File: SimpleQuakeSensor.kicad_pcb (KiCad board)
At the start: 2 copper layers, 39.9 x 22 mm, 37 parts, among them J1 Conn_Coaxial_Small, J2 Conn_Coaxial_Small, J3 Bat -12V GND, J4 Bat +12V, Q1 2N4401, Q2 BF245B, Q3 2N4401

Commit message: Add blocking capacitor
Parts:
- added C14: 10 uF, Capacitor_Tantalum_SMD:CP_EIA-2012-12_Kemet-R, F.Cu at (166.1, 91.7)
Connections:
- C11 pad 1: Net-(J2-In) -> Net-(Q3-C)
- Q3 pad 3: Net-(J2-In) -> Net-(Q3-C)
- R8 pad 1: Net-(J2-In) -> Net-(Q3-C)
- R9 pad 2: Net-(J2-In) -> Net-(Q3-C)
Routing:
- net Net-(J2-In): track 18.6 -> 3.71 mm
- net Net-(Q3-C): track 0.00 -> 14.2 mm

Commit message: Better impedance matching
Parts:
- C10: value 10 nF -> 47 nF
- C11, C7: value 1 nF -> 2.2 nF
- C3: value 1 nF -> 47 nF
- R8: value 10 M -> 2.2 M
- R9: value 100 K -> 22 K
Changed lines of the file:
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@@
 			)
 		)
-		(property "Value" "10 M"
+		(property "Value" "2.2 M"
 			(at 0 1.65 0)
 			(layer "F.Fab")
@@
 			)
 		)
-		(property "Value" "1 nF"
+		(property "Value" "2.2 nF"
 			(at 0 1.68 90)
 			(layer "F.Fab")
@@
 			)
 		)
-		(property "Value" "1 nF"
+		(property "Value" "47 nF"
 			(at 0 1.68 0)
 			(layer "F.Fab")
@@
 			)
 		)
-		(property "Value" "100 K"
+		(property "Value" "22 K"
 			(at 0 1.65 90)
 			(layer "F.Fab")
@@
 			)
 		)
-		(property "Value" "1 nF"
+		(property "Value" "2.2 nF"
 			(at 0 1.68 90)
 			(layer "F.Fab")
@@
 			)
 		)
-		(property "Value" "10 nF"
+		(property "Value" "47 nF"
 			(at 0 1.68 90)
 			(layer "F.Fab")
@@
 	)
 	(segment
-		(start 169.753212 90.621533)
-		(end 166.298467 90.621533)
+		(start 159.543212 94.751533)
+		(end 162.500712 94.751533)
 		(width 1)
 		(layer "F.Cu")
-		(net "Net-(J2-In)")
+		(net "Net-(Q3-C)")
 	)
 	(segment
-		(start 166.298467 90.621533)
-		(end 166.12 90.8)
+		(start 162.500712 94.751533)
+		(end 163.665712 93.586533)
 		(width 1)
 		(layer "F.Cu")
-		(net "Net-(J2-In)")
+		(net "Net-(Q3-C)")
+	)
+	(segment
+		(start 163.623212 95.981533)
+		(end 163.633212 95.971533)
+		(width 1)
+		(layer "F.Cu")
+		(net "Net-(Q3-C)")
+	)
+	(segment
+		(start 158.623212 92.999033)
+		(end 158.790712 92.831533)
+		(width 1)
+		(layer "F.Cu")
+		(net "Net-(Q3-C)")
+	)
+	(segment
+		(start 158.790712 93.999033)
+		(end 159.543212 94.751533)
+		(width 1)
+		(layer "F.Cu")
+		(net "Net-(Q3-C)")
+	)
+	(segment
+		(start 165.113467 93.586533)
+		(end 166.12 92.58)
+		(width 1)
+		(layer "F.Cu")
+		(net "Net-(Q3-C)")
+	)
+	(segment
+		(start 163.633212 94.059033)
+		(end 163.563212 93.989033)
+		(width 1)
+		(layer "F.Cu")
+		(net "Net-(Q3-C)")
+	)
+	(segment
+		(start 163.665712 93.586533)
+		(end 165.113467 93.586533)
+		(width 1)
+		(layer "F.Cu")
+		(net "Net-(Q3-C)")
+	)
+	(segment
+		(start 156.393212 92.999033)
+		(end 158.623212 92.999033)
+		(width 1)
+		(layer "F.Cu")
+		(net "Net-(Q3-C)")
+	)
+	(segment
+		(start 163.633212 95.971533)
+		(end 163.633212 94.059033)
+		(width 1)
+		(layer "F.Cu")
+		(net "Net-(Q3-C)")
+	)
+	(segment
+		(start 158.790712 92.831533)
+		(end 158.790712 93.999033)
+		(width 1)
+		(layer "F.Cu")
+		(net "Net-(Q3-C)")
 	)
 	(segment
@@
 	)
 	(segment
+		(start 169.753212 90.621533)
+		(end 166.298467 90.621533)
+		(width 1)
+		(layer "F.Cu")
+		(net "Net-(J2-In)")
+	)
+	(segment
+		(start 166.298467 90.621533)
+		(end 166.12 90.8)
+		(width 1)
+		(layer "F.Cu")
+		(net "Net-(J2-In)")
+	)
+	(segment
 		(start 148.618212 88.211533)
 		(end 145.493212 88.211533)
@@
 		(net "Net-(J1-Ext)")
 	)
-	(segment
-		(start 159.543212 94.751533)
-		(end 162.500712 94.751533)
-		(width 1)
-		(layer "F.Cu")
-		(net "Net-(Q3-C)")
-	)
-	(segment
-		(start 162.500712 94.751533)
-		(end 163.665712 93.586533)
-		(width 1)
-		(layer "F.Cu")
-		(net "Net-(Q3-C)")
-	)
-	(segment
-		(start 163.623212 95.981533)
-		(end 163.633212 95.971533)
-		(width 1)
-		(layer "F.Cu")
-		(net "Net-(Q3-C)")
-	)
-	(segment
-		(start 158.623212 92.999033)
-		(end 158.790712 92.831533)
-		(width 1)
-		(layer "F.Cu")
-		(net "Net-(Q3-C)")
-	)
-	(segment
-		(start 158.790712 93.999033)
-		(end 159.543212 94.751533)
-		(width 1)
-		(layer "F.Cu")
-		(net "Net-(Q3-C)")
-	)
-	(segment
-		(start 165.113467 93.586533)
-		(end 166.12 92.58)
-		(width 1)
-		(layer "F.Cu")
-		(net "Net-(Q3-C)")
-	)
-	(segment
-		(start 163.633212 94.059033)
-		(end 163.563212 93.989033)
-		(width 1)
-		(layer "F.Cu")
-		(net "Net-(Q3-C)")
-	)
-	(segment
-		(start 163.665712 93.586533)
-		(end 165.113467 93.586533)
-		(width 1)
-		(layer "F.Cu")
-		(net "Net-(Q3-C)")
-	)
-	(segment
-		(start 156.393212 92.999033)
-		(end 158.623212 92.999033)
-		(width 1)
-		(layer "F.Cu")
-		(net "Net-(Q3-C)")
-	)
-	(segment
-		(start 163.633212 95.971533)
-		(end 163.633212 94.059033)
-		(width 1)
-		(layer "F.Cu")
-		(net "Net-(Q3-C)")
-	)
-	(segment
-		(start 158.790712 92.831533)
-		(end 158.790712 93.999033)
-		(width 1)
-		(layer "F.Cu")
-		(net "Net-(Q3-C)")
-	)
 	(zone

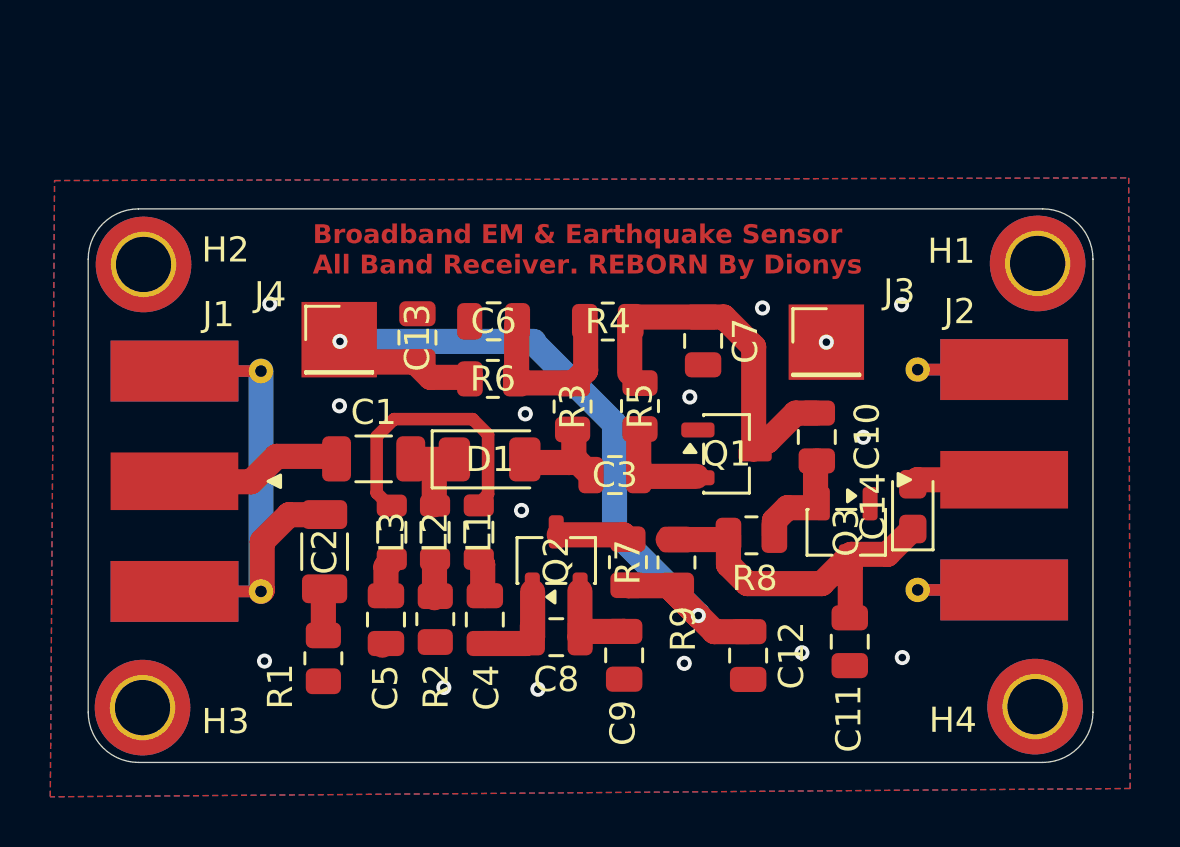
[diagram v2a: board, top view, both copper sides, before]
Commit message: Updating osc, potentiometers, models, licence logo
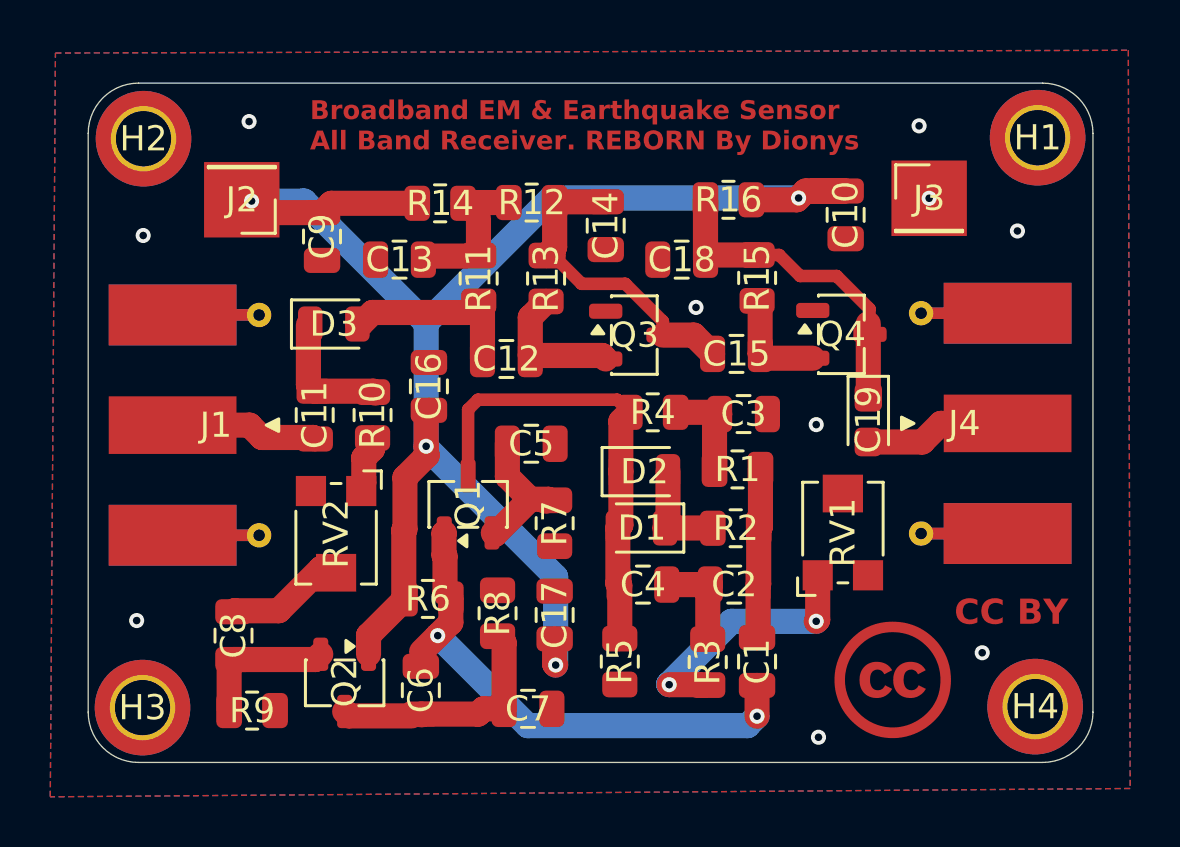
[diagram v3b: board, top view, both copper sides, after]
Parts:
- removed L1, L3: 5 mH, Inductor_SMD:L_0805_2012Metric
- removed L2: 2.2 uH, Inductor_SMD:L_0805_2012Metric
- added C15: 47 nF, Capacitor_SMD:C_0805_2012Metric, F.Cu at (159.1, 85.6)
- added C16: 100 nF, Capacitor_SMD:C_0805_2012Metric, F.Cu at (146.9, 86.9)
- added C17: 100 nF, Capacitor_SMD:C_0805_2012Metric, F.Cu at (151.9, 96.0)
- added C18: 2.2 nF, Capacitor_SMD:C_0805_2012Metric, F.Cu at (156.9, 81.9)
- added C19: 10 uF, Capacitor_Tantalum_SMD:CP_EIA-2012-15_AVX-P, F.Cu at (164.3, 88.2)
- added D2: 1N914WT, Diode_SMD:D_0805_2012Metric, F.Cu at (155.4, 90.3)
- added D3: 1N5711, Diode_SMD:D_0805_2012Metric, F.Cu at (143.1, 84.4)
- added Q4: 2N4401, Package_TO_SOT_SMD:SOT-23-3, F.Cu at (163.3, 84.8)
- added R10: 10k, Resistor_SMD:R_0805_2012Metric, F.Cu at (144.6, 88.0)
- added R11: 10 M, Resistor_SMD:R_0805_2012Metric, F.Cu at (148.9, 82.6)
- added R12: 100 K, Resistor_SMD:R_0805_2012Metric, F.Cu at (151.0, 79.6)
- added R13: 10 M, Resistor_SMD:R_0805_2012Metric, F.Cu at (151.5, 82.6)
- added R14: 10 K, Resistor_SMD:R_0805_2012Metric, F.Cu at (147.3, 79.6)
- added R15: 2.2 M, Resistor_SMD:R_0805_2012Metric, F.Cu at (159.9, 82.6)
- added R16: 22 K, Resistor_SMD:R_0805_2012Metric, F.Cu at (158.8, 79.5)
- added RV1: 1K, Potentiometer_SMD:Potentiometer_Bourns_TC33X_Vertical, F.Cu at (163.3, 92.6)
- added RV2: 1K, Potentiometer_SMD:Potentiometer_Bourns_TC33X_Vertical, F.Cu at (143.2, 92.9)
- C1: value 220 pF -> 100 nF; footprint Capacitor_SMD:C_1206_3216Metric -> Capacitor_SMD:C_0805_2012Metric
- C10, C9: value 47 nF -> 100 nF
- C11: value 2.2 nF -> 220 pF
- C12: value 100 nF -> 47 nF
- C14: value 10 uF -> 2.2 nF; footprint Capacitor_Tantalum_SMD:CP_EIA-2012-12_Kemet-R -> Capacitor_SMD:C_0805_2012Metric
- C2: value 220 pF -> 1nF; footprint Capacitor_SMD:C_1206_3216Metric -> Capacitor_SMD:C_0805_2012Metric
- C3: value 47 nF -> 2nF
- C4: value 10 nF -> 1nF
- C5: value 10 nF -> 470nF
- C6: value 100 nF -> 10nF
- C7: value 2.2 nF -> 22pF
- C8: value 47 nF -> 100nF
- D1: value 1N5711 -> 1N914WT; footprint Diode_SMD:D_1206_3216Metric -> Diode_SMD:D_0805_2012Metric
- J2: value Conn_Coaxial_Small -> Bat +12V; footprint Connector_Coaxial:SMA_Molex_73251-1153_EdgeMount_Horizontal -> fmd-laser-libs:PinHeader_1x01_P2.54mm_Vertical_2_FMD
- J4: value Bat +12V -> Conn_Coaxial_Small; footprint fmd-laser-libs:PinHeader_1x01_P2.54mm_Vertical_2_FMD -> Connector_Coaxial:SMA_Molex_73251-1153_EdgeMount_Horizontal
- Q1: value 2N4401 -> MMBFJ201
- Q2: value BF245B -> MMBFJ201
- R1: value 10k -> 6.65K
- R2: value 10k -> 470K
- R3: value 10 M -> 2.7K
- R4: value 100 K -> 6.65K
- R5: value 10 M -> 1M
- R6: value 10 K -> 10K
- R7: value 100 K -> 2.2K
- R8: value 2.2 M -> 1M
- R9: value 22 K -> 10K
- moved J2 30.7 mm to (139.4, 79.5)
- moved J4 25.1 mm to (168.2, 88.4), turned to 180 degrees
- moved C11 23.1 mm to (142.3, 88.0), turned to 90 degrees
- moved C9 20.5 mm to (142.6, 81.0)
- moved R1 18.1 mm to (159.2, 90.2), turned to 180 degrees
- moved R9 17.9 mm to (139.8, 99.8), turned to 0 degrees
- moved C1 17.2 mm to (159.9, 97.8), turned to 90 degrees
- moved C14 16.5 mm to (153.9, 80.5), turned to -90 degrees
- moved C2 16.3 mm to (159.0, 94.8), turned to 180 degrees
- moved C7 16.2 mm to (150.8, 99.7), turned to 0 degrees
- moved C12 15.2 mm to (150.0, 85.8), turned to 0 degrees
- moved C6 15.0 mm to (146.6, 99.0), turned to -90 degrees
- moved C8 12.8 mm to (139.1, 96.8), turned to 90 degrees
- moved R2 12.5 mm to (159.1, 92.5), turned to 180 degrees
- moved Q3 11.5 mm to (155.0, 84.9), turned to 0 degrees
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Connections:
- C1 pad 1: Net-(J1-In) -> Net-(Q1-D)
- C1 pad 2: Net-(D1-K) -> Net-(C1-Pad2)
- C10 pad 1: Net-(Q3-B) -> 0
- C10 pad 2: Net-(Q1-C) -> /Bat +12V
- C11 pad 1: Net-(Q3-C) -> Net-(J1-In)
- C11 pad 2: 0 -> Net-(D3-K)
- C12 pad 1: 0 -> Net-(D3-A)
- C12 pad 2: Net-(BT1-+) -> Net-(Q3-B)
- C13 pad 1: Net-(BT1-+) -> Net-(C13-Pad1)
- C14 pad 2: Net-(J2-In) -> 0
- C2 pad 1: Net-(J1-Ext) -> Net-(C1-Pad2)
- C3 pad 1: Net-(D1-A) -> 0
- C3 pad 2: Net-(Q1-B) -> Net-(C3-Pad2)
- C4 pad 1: Net-(C4-Pad1) -> Net-(C2-Pad2)
- C4 pad 2: Net-(Q2-G) -> Net-(D1-A)
- C5 pad 1: Net-(C5-Pad1) -> 0
- C5 pad 2: 0 -> Net-(Q1-S)
- C6 pad 1: Net-(C6-Pad1) -> Net-(Q1-D)
- C6 pad 2: 0 -> Net-(Q2-G)
- C7 pad 1: Net-(Q1-C) -> Net-(Q2-G)
- C8 pad 2: Net-(Q2-G) -> Net-(C8-Pad2)
- C9 pad 1: Net-(Q2-S) -> /Bat +12V
- J1 pad 2: Net-(J1-Ext) -> 0
- J2 pad 1: Net-(J2-In) -> /Bat +12V
- J4 pad 1: Net-(BT1-+) -> Net-(J4-In)
- Q1 pad 1: 0 -> Net-(Q1-D)
- Q1 pad 2: Net-(Q1-B) -> Net-(Q1-S)
- Q1 pad 3: Net-(Q1-C) -> Net-(D1-A)
- Q2 pad 1: Net-(Q2-G) -> /Bat +12V
- Q2 pad 3: Net-(Q2-D) -> Net-(Q2-G)
- R1 pad 1: Net-(C2-Pad2) -> Net-(C1-Pad2)
- R1 pad 2: 0 -> Net-(C3-Pad2)
- R2 pad 1: 0 -> Net-(C1-Pad2)
- R2 pad 2: Net-(L2-Pad1) -> Net-(D1-K)
- R3 pad 1: Net-(C6-Pad1) -> Net-(C2-Pad2)
- R3 pad 2: Net-(D1-A) -> Net-(R3-Pad2)
- R4 pad 1: Net-(C6-Pad1) -> Net-(C3-Pad2)
- R4 pad 2: Net-(Q1-C) -> Net-(D1-A)
- R5 pad 1: Net-(Q1-C) -> Net-(D1-A)
- R5 pad 2: Net-(Q1-B) -> 0
- R6 pad 1: Net-(C6-Pad1) -> /Bat +12V
- R6 pad 2: Net-(BT1-+) -> Net-(Q1-D)
- R7 pad 1: Net-(Q2-D) -> Net-(Q1-S)
- R7 pad 2: Net-(BT1-+) -> 0
- R8 pad 1: Net-(Q3-C) -> Net-(Q2-G)
- R8 pad 2: Net-(Q3-B) -> 0
- R9 pad 1: Net-(BT1-+) -> Net-(Q2-S)
- R9 pad 2: Net-(Q3-C) -> 0
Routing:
- net /Bat +12V: track 0.00 -> 65.9 mm, vias 0 -> 4
- net Net-(BT1-+): track 34.5 -> 0.00 mm, vias 2 -> 0
- net Net-(Q1-D): track 0.00 -> 20.9 mm, vias 0 -> 2
- net Net-(Q1-C): track 14.7 -> 0.00 mm
- net Net-(D1-A): track 4.30 -> 18.7 mm
- net Net-(J1-Ext): track 13.8 -> 0.00 mm
- net Net-(Q4-C): track 0.00 -> 13.3 mm
- net Net-(L1-Pad2): track 11.1 -> 0.00 mm
- net Net-(R3-Pad2): track 0.00 -> 10.3 mm, vias 0 -> 2
- net Net-(D3-A): track 0.00 -> 7.54 mm
- net Net-(C6-Pad1): track 7.18 -> 0.00 mm
- net Net-(C1-Pad2): track 0.00 -> 6.75 mm
- net Net-(J4-In): track 0.00 -> 5.85 mm
- net Net-(Q1-S): track 0.00 -> 5.57 mm
- net Net-(Q2-G): track 3.81 -> 9.18 mm
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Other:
- board size 39.9 x 22 mm -> 39.9 x 27 mm
- board text added: "CC BY"

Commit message: PCB update
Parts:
- R14: value 10 K -> 1 K
- moved J2 0.39 mm to (139.7, 79.2)
- moved Q1 0.20 mm to (148.4, 91.8)
- moved J3 0.17 mm to (166.9, 79.3)
- moved C9 0.16 mm to (142.8, 81.0)
- moved R3 0.14 mm to (157.8, 97.8)
- moved R13 0.09 mm to (151.4, 82.6)
- moved RV2 0.08 mm to (143.1, 92.9)
- moved C7 0.08 mm to (150.8, 99.8)
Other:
- board text added: "+12v"
- board text added: "GND"
- board text added: "Input (probes)"
- board text added: "Output"

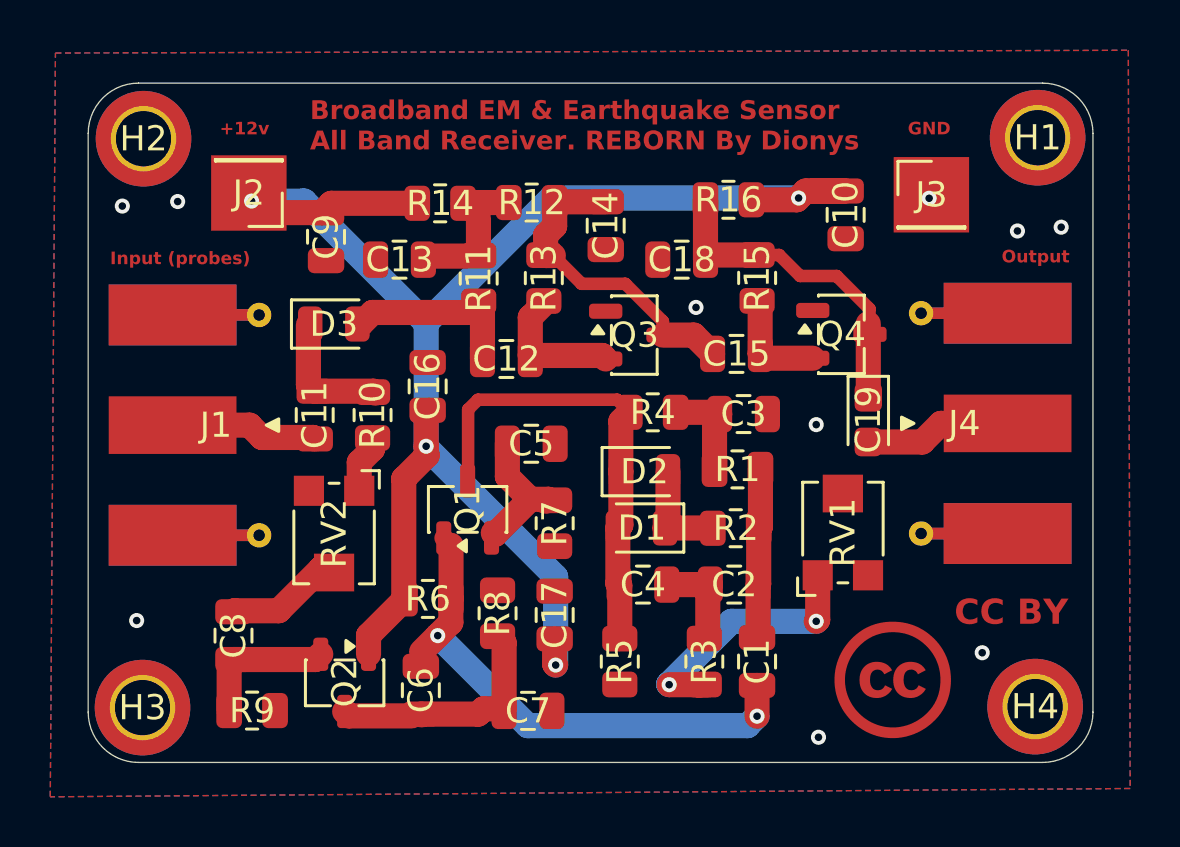
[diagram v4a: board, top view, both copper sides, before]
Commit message: Updating PCB grid
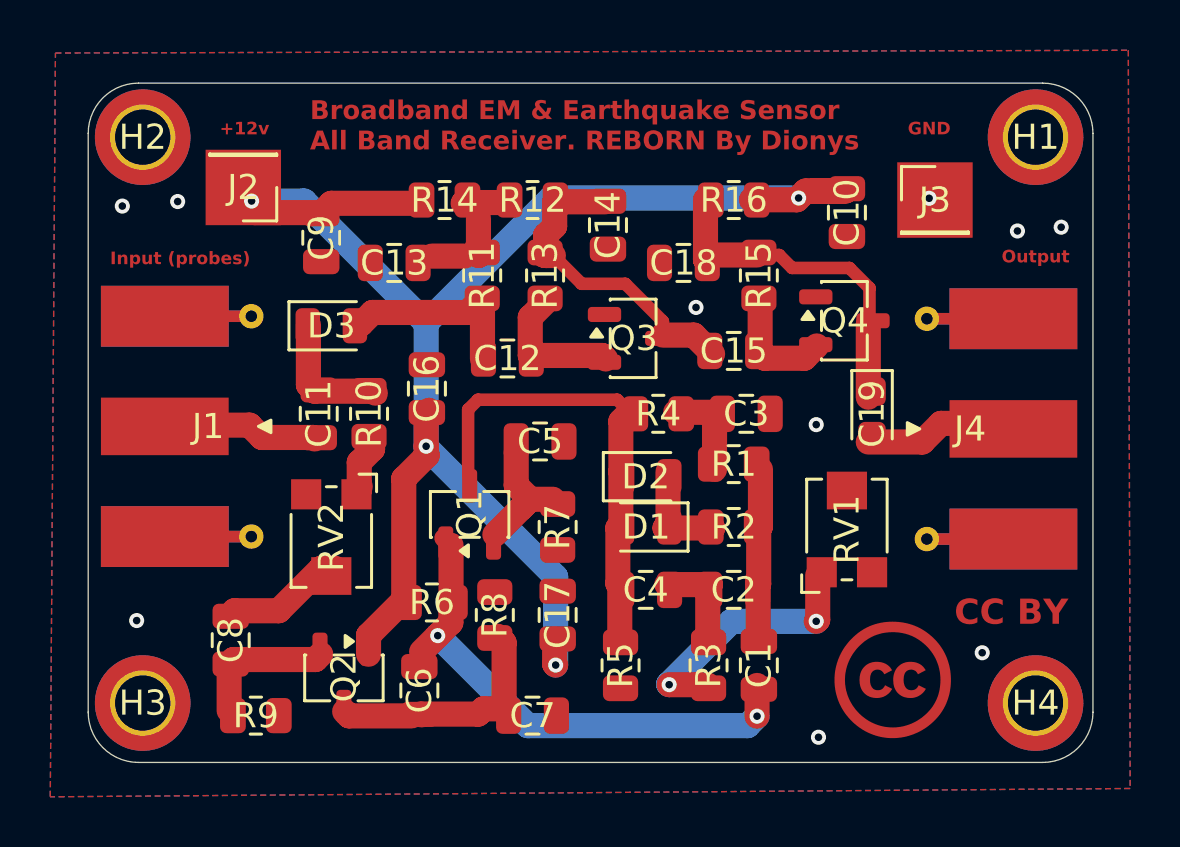
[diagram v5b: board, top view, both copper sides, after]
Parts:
- moved Q4 0.55 mm to (163.4, 84.3)
- moved C5 0.36 mm to (151.3, 89.1)
- moved J4 0.32 mm to (168.4, 88.6)
- moved J1 0.31 mm to (138.1, 88.5)
- moved J2 0.31 mm to (139.5, 79.0)
- moved C19 0.27 mm to (164.5, 88.0)
- moved C7 0.26 mm to (151.0, 100.0)
- moved R1 0.26 mm to (159.0, 90.0)
- moved J3 0.25 mm to (167.0, 79.5)
- moved R9 0.25 mm to (140.0, 100.0)
- moved C13 0.25 mm to (145.5, 82.0)
- moved C4 0.24 mm to (155.5, 95.0)
- moved R4 0.23 mm to (156.0, 88.0)
- moved R3 0.23 mm to (158.0, 98.0)
- moved R14 0.22 mm to (147.5, 79.5)
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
